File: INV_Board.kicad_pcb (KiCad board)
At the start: 2 copper layers, 100 x 50 mm, 125 parts, among them J1 USB_B_Micro, J10 Conn_01x02_Male, J11 Conn_01x04_Male, J2 Conn_01x02_Male, J3 Conn_01x02_Male, J4 Conn_01x02_Male, J5 Conn_01x04_Male, J6 Conn_01x03_Male, J7 Conn_01x03_Male, J8 Conn_ARM_JTAG_SWD_10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

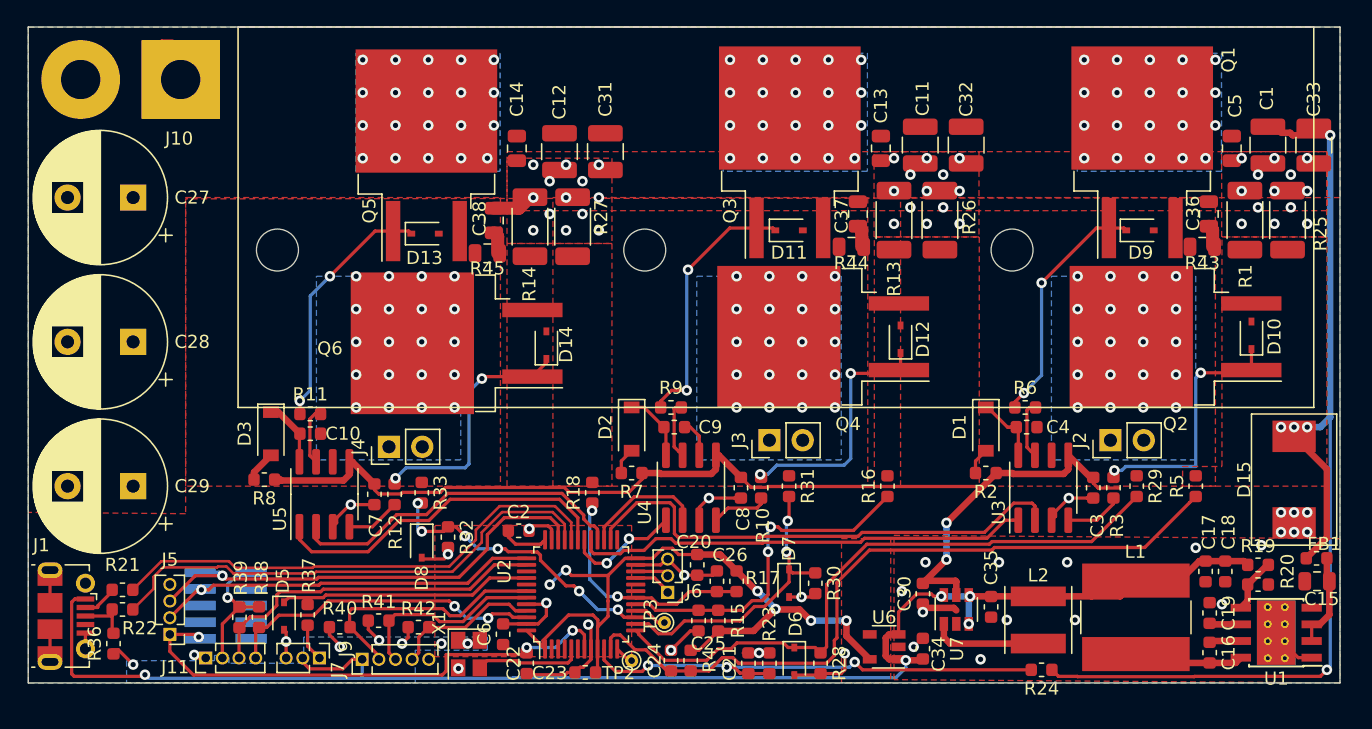
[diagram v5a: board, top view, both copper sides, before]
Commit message: Added input resistors on Hall lines, added TVS protection on input lines I2C, USB UART protected with 0402 resistors, since no space... ToDo... fit 0603 or learn to solder 0402... ugh.
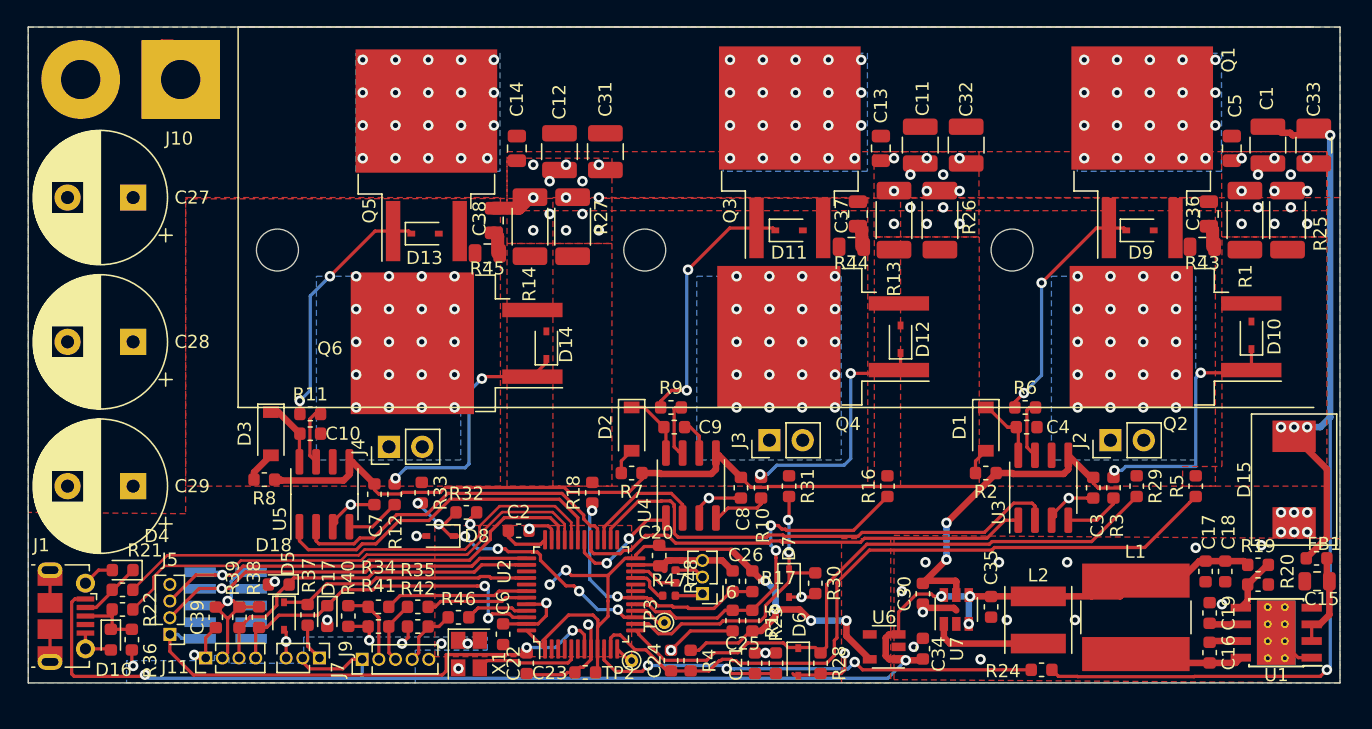
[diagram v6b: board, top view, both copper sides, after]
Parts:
- added C39: C_0.1uF_25V, Capacitor_SMD:C_0603_1608Metric, F.Cu at (54.3, 73.0)
- added D16: D_TVS, Diode_SMD:D_0603_1608Metric, F.Cu at (46.3, 74.7)
- added D17: D_TVS, Diode_SMD:D_0603_1608Metric, F.Cu at (62.8, 72.9)
- added D18: D_TVS, Diode_SMD:D_0603_1608Metric, F.Cu at (59.1, 70.5)
- added D4: D_TVS, Diode_SMD:D_0603_1608Metric, F.Cu at (47.2, 69.4)
- added R34: R_4k7, Resistor_SMD:R_0603_1608Metric, F.Cu at (66.7, 72.2)
- added R35: R_4k7, Resistor_SMD:R_0603_1608Metric, F.Cu at (69.7, 72.2)
- added R46: R_4k7, Resistor_SMD:R_0603_1608Metric, F.Cu at (72.8, 73.0)
- added R47: R_100, Resistor_SMD:R_0402_1005Metric, F.Cu at (88.8, 71.3)
- added R48: R_100, Resistor_SMD:R_0402_1005Metric, F.Cu at (89.3, 69.9)
- moved C20 2.99 mm to (88.1, 68.3)
- moved J6 2.65 mm to (91.4, 71.2)
- moved C25 2.60 mm to (93.7, 73.2)
- moved R15 2.60 mm to (95.2, 73.2)
- moved R32 2.35 mm to (73.4, 65.0), turned to 0 degrees
- moved D8 1.52 mm to (71.4, 66.8), turned to 180 degrees
- moved R36 1.43 mm to (47.9, 74.7)
- moved C26 1.20 mm to (93.7, 70.2)
- moved R17 1.20 mm to (95.2, 70.2)
- moved R40 1.07 mm to (64.4, 72.9), turned to 90 degrees
- moved C21 0.50 mm to (95.4, 76.5)
- moved R23 0.50 mm to (97.0, 76.5)
- moved R41 0.45 mm to (66.7, 73.7)
- moved D6 0.30 mm to (98.7, 76.4)
- moved U4 0.17 mm to (90.5, 63.0)
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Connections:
- J6 pad 1: STTx -> Net-(J6-Pad1)
- J6 pad 2: STRx -> Net-(J6-Pad2)
- J9 pad 2: /Hall1 -> Net-(J9-Pad2)
- J9 pad 3: /Hall2 -> Net-(J9-Pad3)
- J9 pad 4: /Hall3 -> Net-(J9-Pad4)
- R40 pad 2: /Hall1 -> Net-(J9-Pad2)
- R41 pad 2: /Hall2 -> Net-(J9-Pad3)
- R42 pad 2: /Hall3 -> Net-(J9-Pad4)
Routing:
- net GND: track 70.4 -> 80.9 mm, vias 72 -> 74
- net /Hall1: track 19.2 -> 11.0 mm
- net /Hall2: track 14.7 -> 7.79 mm
- net /Hall3: track 11.4 -> 4.78 mm
- net Net-(J9-Pad2): track 0.00 -> 6.10 mm
- net Net-(J9-Pad3): track 0.00 -> 5.17 mm
- net Net-(J9-Pad4): track 0.00 -> 4.75 mm
- net +3V3: track 75.3 -> 77.6 mm, vias 13 -> 12
- net Net-(J6-Pad2): track 0.00 -> 2.27 mm
- net I2CSDA: track 24.5 -> 26.7 mm
- net USBD-: track 2.74 -> 4.88 mm
- net Net-(J6-Pad1): track 0.00 -> 2.13 mm
- net ISW_MCU: track 18.3 -> 20.1 mm
- net SWCLK: track 29.1 -> 30.7 mm
- net USBD+: track 4.02 -> 5.62 mm
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
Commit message: Update R values on power and switch lines to 1k5 and 47k 0805 to enable voltages up to 3.3*48.5/1.5=106V. Add power LEDs and extra 5V cap near USB. Change all text to 0.8mm to make it tidier.
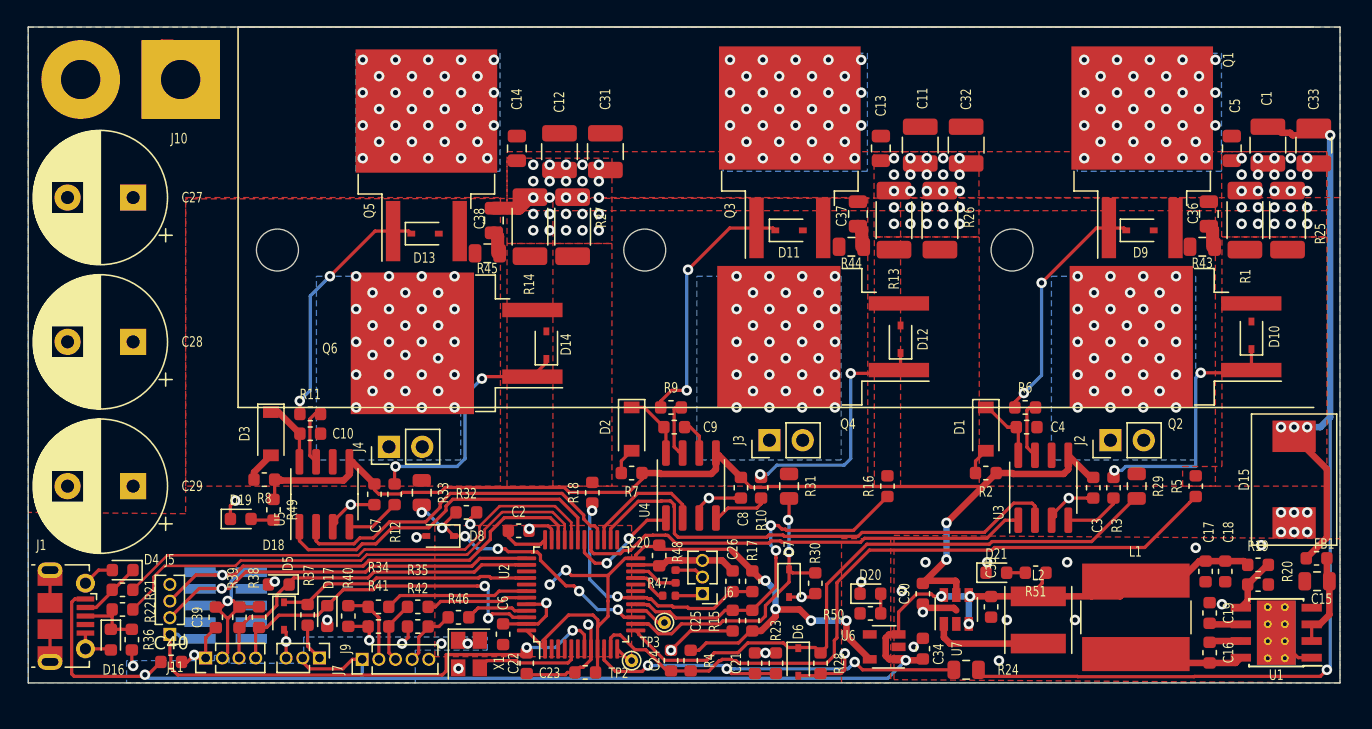
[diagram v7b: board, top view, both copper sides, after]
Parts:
- added C40: C_10uF_16V, Capacitor_SMD:C_0603_1608Metric, F.Cu at (50.9, 76.4)
- added D19: LED_Small, LED_SMD:LED_0603_1608Metric, F.Cu at (56.2, 65.5)
- added D20: LED_Small, LED_SMD:LED_0603_1608Metric, F.Cu at (104.2, 71.2)
- added D21: LED_Small, LED_SMD:LED_0603_1608Metric, F.Cu at (113.8, 69.6)
- added R49: R_4k7, Resistor_SMD:R_0603_1608Metric, F.Cu at (58.7, 64.8)
- added R50: R_4k7, Resistor_SMD:R_0603_1608Metric, F.Cu at (104.2, 72.7)
- added R51: R_4k7, Resistor_SMD:R_0603_1608Metric, F.Cu at (116.8, 69.6)
- R16, R18, R5: value R_680 -> R_150
- R23, R28, R30, R32: value R_4k7 -> R_1k5
- R24, R29, R31, R33: footprint Resistor_SMD:R_0603_1608Metric -> Resistor_SMD:R_0805_2012Metric
- moved R24 5.75 mm to (111.5, 77.0)
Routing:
- net Vsense_MCU: track 38.4 -> 32.6 mm
- net +VDC: track 83.5 -> 89.1 mm, vias 65 -> 102
- net +5V: track 120.8 -> 124.4 mm
- net GND: track 80.9 -> 83.7 mm, vias 74 -> 112
- net Net-(D19-Pad2): track 0.00 -> 1.75 mm
- net Net-(D20-Pad2): track 0.00 -> 1.50 mm
- net Net-(D21-Pad2): track 0.00 -> 1.42 mm
- net +12V: track 88.1 -> 87.0 mm
- net #RES: track 39.6 -> 40.3 mm
- net SWW: vias 20 -> 32
- net SWV: vias 20 -> 32
- net SWU: vias 20 -> 32

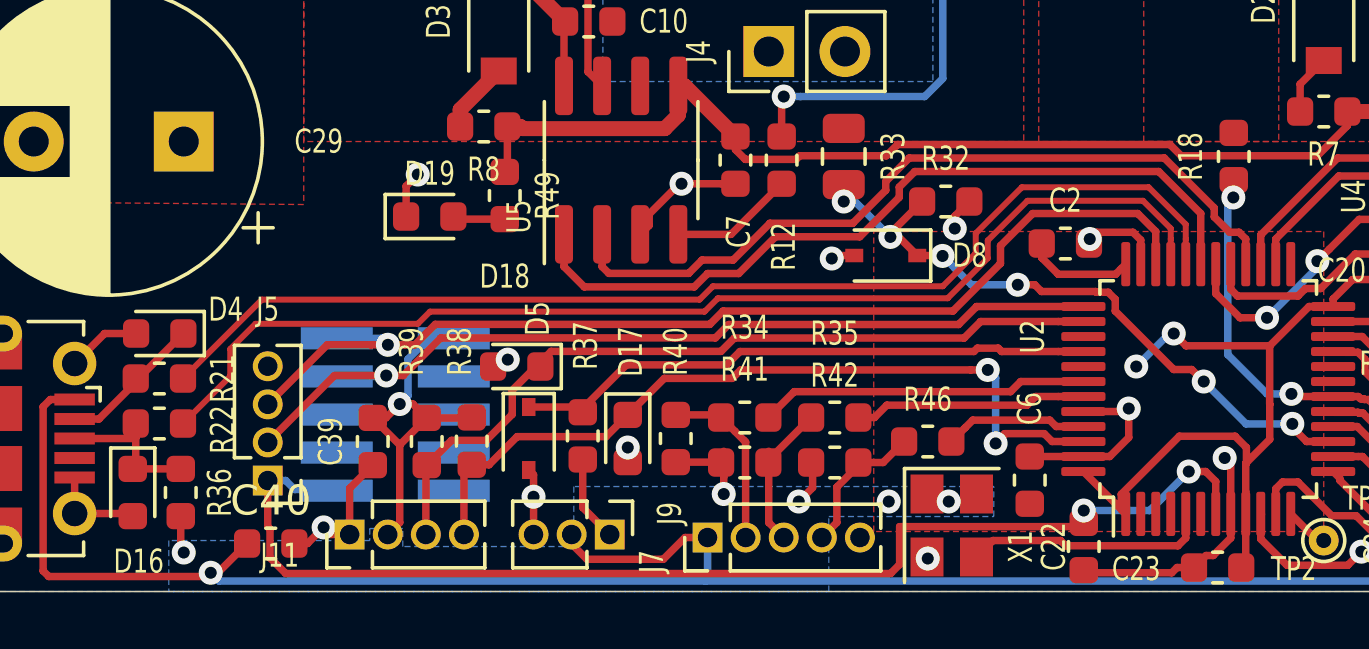
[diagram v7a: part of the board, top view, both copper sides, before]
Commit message: Added SWO line to the JTAG header to aid debugging and live variable tracking. Will have to manually mod with wire the first set of boards ordered.
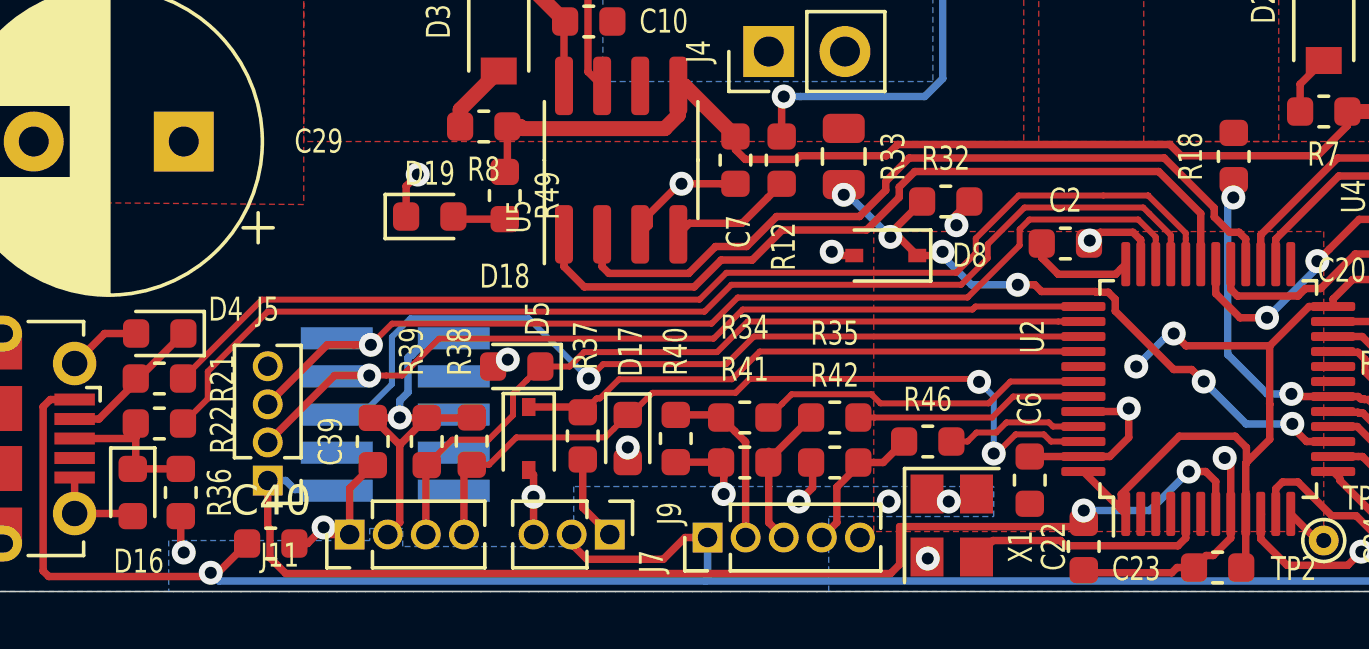
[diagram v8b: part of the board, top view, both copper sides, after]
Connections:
- J8 pad 6: Net-(J8-Pad6) -> SWO
- U2 pad 39: Net-(U2-Pad39) -> SWO
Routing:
- net SWO: track 0.00 -> 29.6 mm, vias 0 -> 1
- net SWDIO: track 35.7 -> 34.8 mm
- net SWCLK: track 30.7 -> 30.2 mm
